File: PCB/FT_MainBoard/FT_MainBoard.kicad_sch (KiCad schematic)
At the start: 38 parts, among them SW1 SW_Push

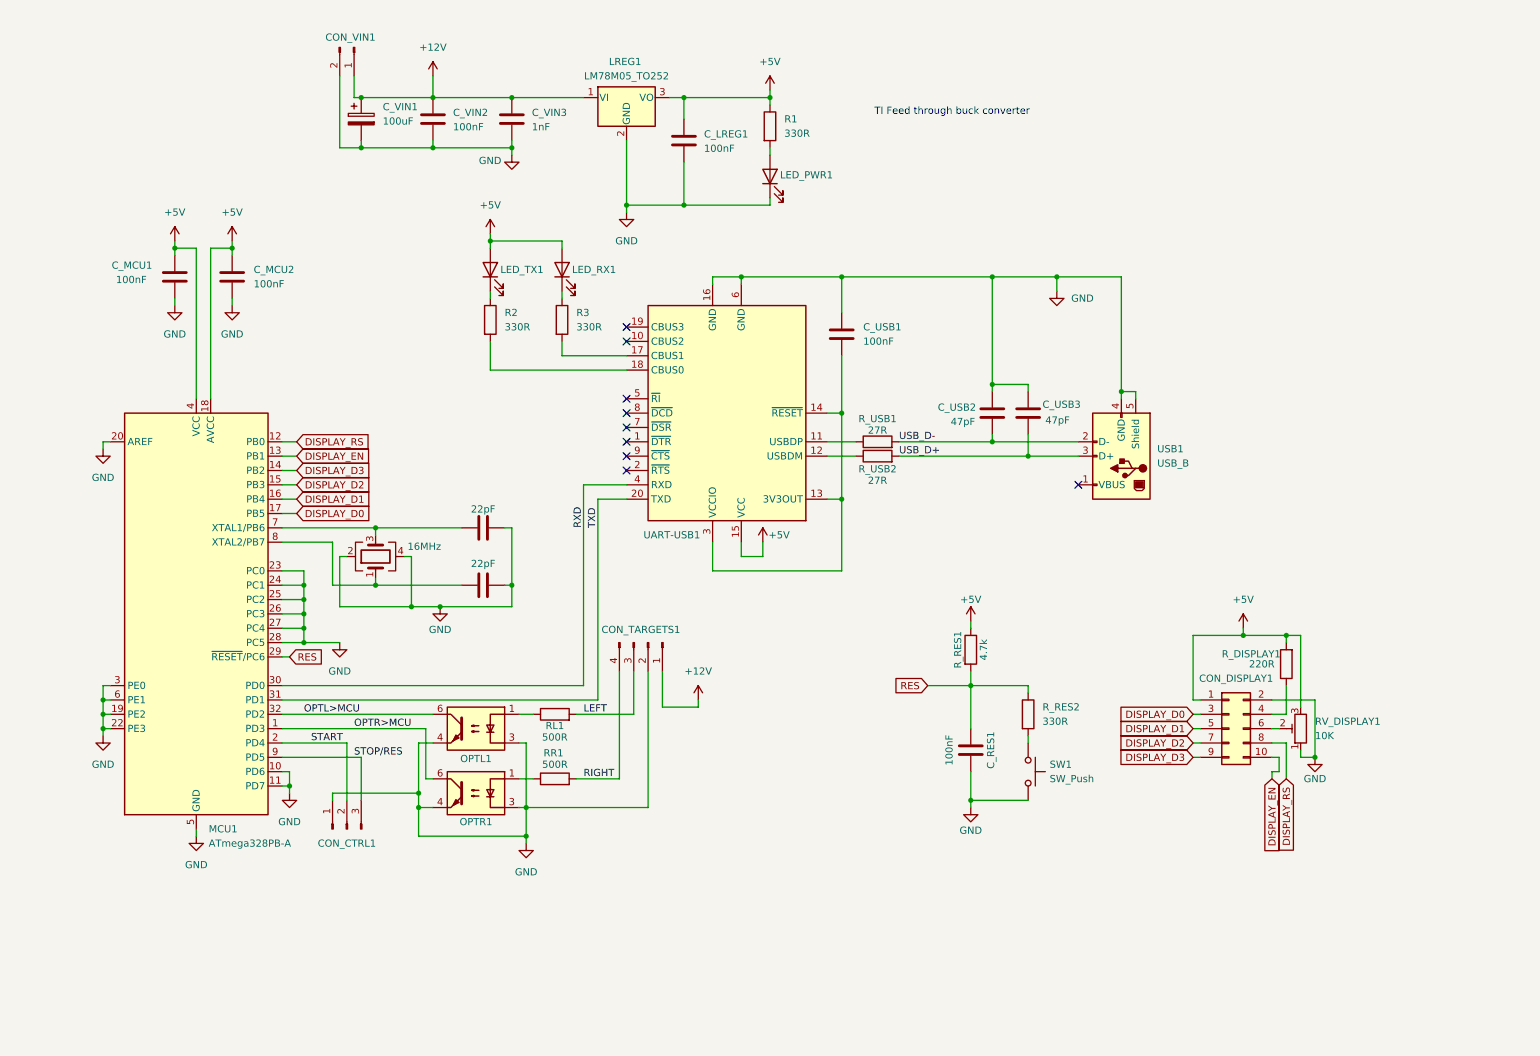
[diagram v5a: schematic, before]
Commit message: hall and switch done
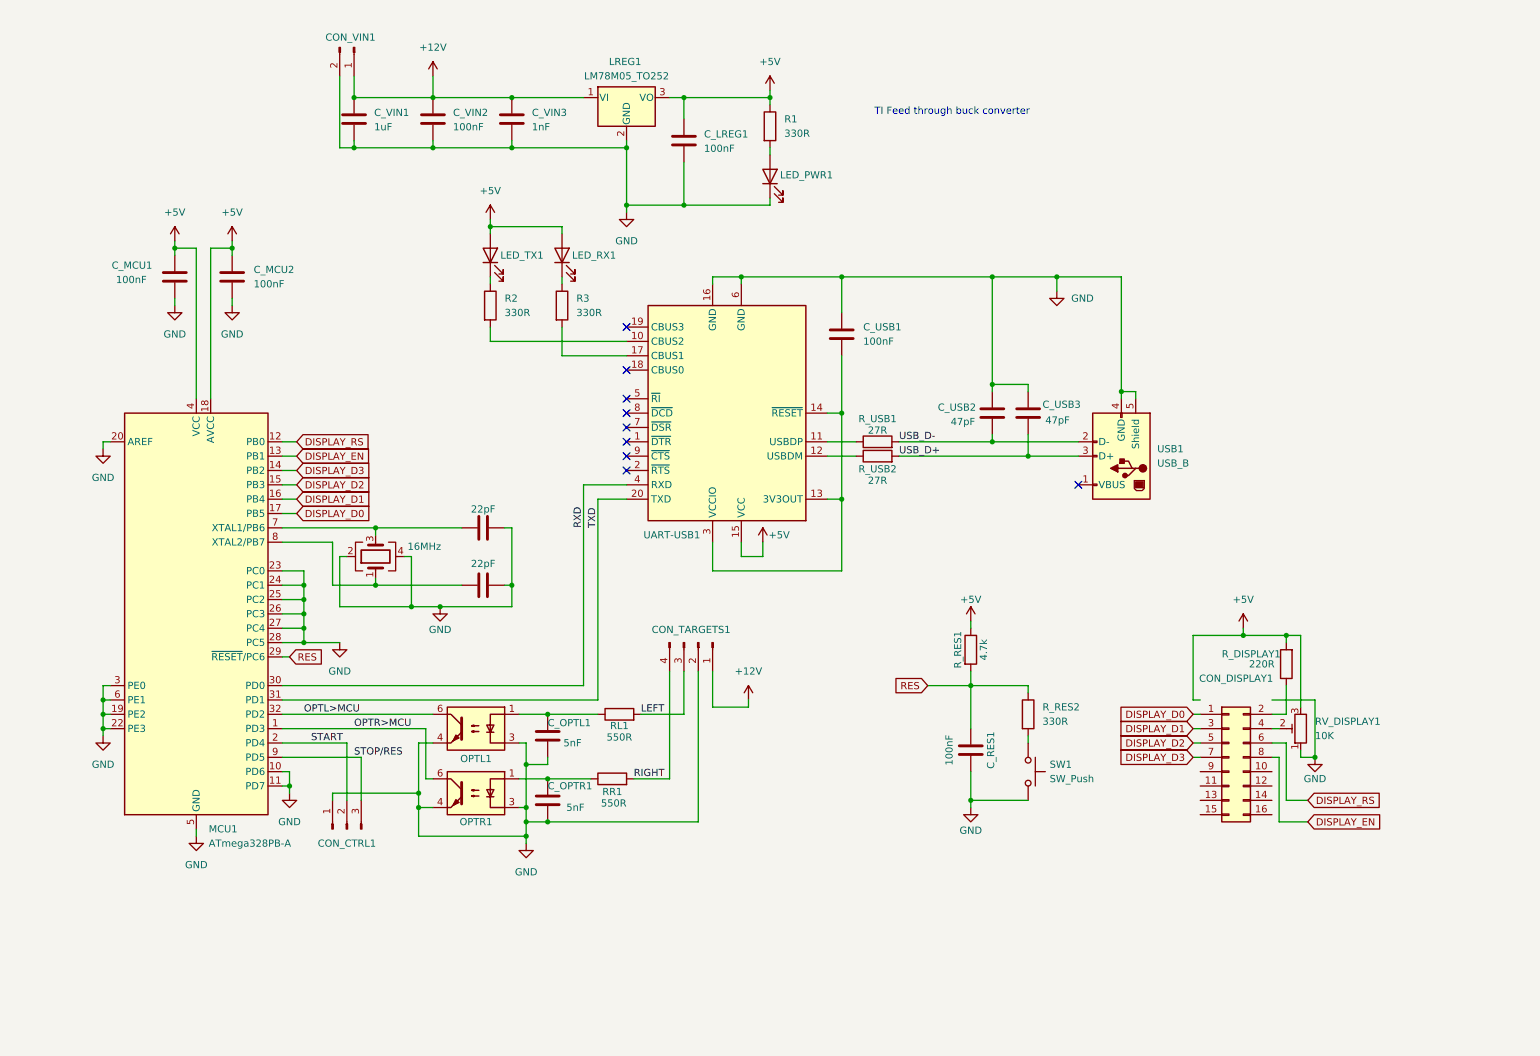
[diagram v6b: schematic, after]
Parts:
- removed CON_DISPLAY1: Conn_02x05_Odd_Even, Connector_PinHeader_2.54mm:PinHeader_2x05_P2.54mm_Horizontal, symbol Connector_Generic:Conn_02x05_Odd_Even
- removed C_VIN1: 100uF, Capacitor_SMD:CP_Elec_5x5.8, symbol Device:C_Polarized
- added CON_DISPLAY1: Conn_02x08_Odd_Even, Connector_PinHeader_2.54mm:PinHeader_2x08_P2.54mm_Vertical, symbol Connector_Generic:Conn_02x08_Odd_Even
- added C_OPTL1, C_OPTR1: 5nF, Capacitor_SMD:C_0603_1608Metric, symbol Device:C
- added C_VIN1: 1uF, Capacitor_SMD:C_0603_1608Metric, symbol Device:C
- RL1, RR1: value 500R -> 550R
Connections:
- net +12V: now also C_VIN1.1
- net DISPLAY_D0: now also CON_DISPLAY1.1 (Pin_1)
- net DISPLAY_D1: now also CON_DISPLAY1.3 (Pin_3)
- net DISPLAY_D2: now also CON_DISPLAY1.5 (Pin_5)
- net DISPLAY_D3: now also CON_DISPLAY1.7 (Pin_7)
- net DISPLAY_EN: now also CON_DISPLAY1.8 (Pin_8)
- net DISPLAY_RS: now also CON_DISPLAY1.6 (Pin_6)
- net GND: now also C_OPTL1.2, C_OPTR1.2, C_VIN1.2
- net at OPTL1.1, RL1.1: now also C_OPTL1.1
- net at R_DISPLAY1.1: now also CON_DISPLAY1.2 (Pin_2)
- net at RV_DISPLAY1.2: now also CON_DISPLAY1.4 (Pin_4)
- net at OPTR1.1, RR1.1: now also C_OPTR1.1
- net at R2.2: now also UART-USB1.10 (CBUS2); no longer UART-USB1.18 (CBUS0)
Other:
- moved on the sheet: CON_TARGETS1, LED_RX1, LED_TX1, R2, R3, RL1, RR1

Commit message: main board update
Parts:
- removed CON_CTRL1: Conn_01x03_Pin, Connector_PinHeader_2.54mm:PinHeader_1x03_P2.54mm_Horizontal, symbol Connector:Conn_01x03_Pin
- removed CON_DISPLAY1: Conn_02x08_Odd_Even, Connector_PinHeader_2.54mm:PinHeader_2x08_P2.54mm_Vertical, symbol Connector_Generic:Conn_02x08_Odd_Even
- removed RV_DISPLAY1: 10K, Potentiometer_SMD:Potentiometer_Bourns_TC33X_Vertical, symbol Device:R_Potentiometer_Trim
- removed R_DISPLAY1: 220R, Resistor_SMD:R_0603_1608Metric, symbol Device:R
- added CON_CTRL1: Conn_01x04_Pin, Connector_PinHeader_2.54mm:PinHeader_1x04_P2.54mm_Horizontal, symbol Connector:Conn_01x04_Pin
- added C_RES2: 100nF, Capacitor_SMD:C_0603_1608Metric, symbol Device:C
- added SW2: SW_SPST, Button_Switch_THT:SW_DIP_SPSTx01_Slide_9.78x4.72mm_W7.62mm_P2.54mm, symbol Switch:SW_SPST
- C_OPTL1, C_OPTR1: value 5nF -> 100nF
- R_RES1: value 4.7k -> 10K
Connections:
- net GND: now also CON_CTRL1.1 (Pin_1); no longer MCU1.10 (PD6)
- net RES: now also SW2.1 (A)
- net START: now also CON_CTRL1.2 (Pin_2)
- net at LED_TX1.1 (K): now also R3.2; no longer R2.1
- net at LED_RX1.1 (K): now also R2.1; no longer R3.1
- net at UART-USB1.17 (CBUS1): now also R3.1; no longer R3.2
- net DTR: now reaches UART-USB1.1 (~{DTR})
- net DTR: now also C_RES2.1
- net LEFT renamed IN_LEFT
- net OPTL>MCU renamed OPTL
- net OPTR>MCU renamed OPTR
- net RIGHT renamed IN_RIGHT
- net RXD renamed MCU_RX
- net MCU_RX: now also UART-USB1.20 (TXD); no longer UART-USB1.4 (RXD)
- net STOP/RES renamed STOP
- net STOP: now also CON_CTRL1.3 (Pin_3)
- net TXD renamed MCU_TX
- net MCU_TX: now also UART-USB1.4 (RXD); no longer UART-USB1.20 (TXD)
- new net: C_RES2.2, SW2.2 (B)
- new net RESET: CON_CTRL1.4 (Pin_4), MCU1.10 (PD6)
- no-connect marks 9 -> 8
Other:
- note added: "Power"
- note added: "Reset"
- note added: "Target inputs"
- note added: "USB to serial"
- note removed: "TI Feed through buck converter"
- moved on the sheet: CON_TARGETS1, CON_VIN1, C_LREG1, C_MCU1, C_MCU2, C_OPTL1, C_OPTR1, C_RES1, C_USB1, C_USB2, C_USB3, C_VIN1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

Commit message: main board update
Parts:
- added C_IN1, C_IN2, C_IN3: 100n, Capacitor_SMD:C_0603_1608Metric, symbol Device:C
- added R_IN1, R_IN2, R_IN3, R_IN4, R_IN5, R_IN6: 1000R, Resistor_SMD:R_0603_1608Metric, symbol Device:R
- added SCH1: 74HC3G14DP,125, Package_SO:MSOP-8_3x3mm_P0.65mm, symbol 74HC3G14DP,125:74HC3G14DP,125
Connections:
- net +5V: now also R_IN4.1, R_IN5.1, R_IN6.1, SCH1.8 (VCC)
- net GND: now also C_IN1.2, C_IN2.2, C_IN3.2, SCH1.4 (GND)
- net RESET: now also SCH1.2 (3Y); no longer CON_CTRL1.4 (Pin_4)
- net START: now also SCH1.7 (1Y); no longer CON_CTRL1.2 (Pin_2)
- net STOP: now also SCH1.5 (2Y); no longer CON_CTRL1.3 (Pin_3)
- new net: CON_CTRL1.4 (Pin_4), R_IN3.1, R_IN6.2
- new net: C_IN3.1, R_IN3.2, SCH1.6 (3A)
- new net: CON_CTRL1.2 (Pin_2), R_IN1.1, R_IN4.2
- new net: CON_CTRL1.3 (Pin_3), R_IN2.1, R_IN5.2
- new net: C_IN1.1, R_IN1.2, SCH1.1 (1A)
- new net: C_IN2.1, R_IN2.2, SCH1.3 (2A)
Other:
- note added: "Button inputs"
- moved on the sheet: CON_CTRL1
